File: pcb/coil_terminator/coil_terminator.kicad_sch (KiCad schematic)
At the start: 2 parts, among them J1 Conn_Coaxial

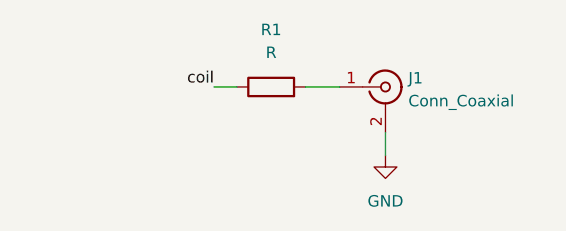
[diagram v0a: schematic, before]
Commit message: added models for compensating coil loss
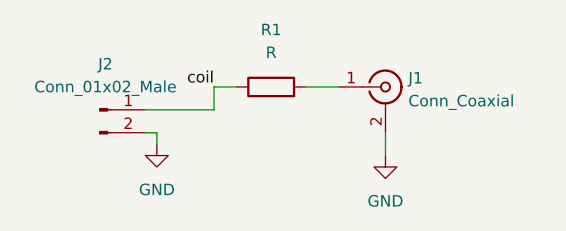
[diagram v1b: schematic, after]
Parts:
- added J2: Conn_01x02_Male, Connector_PinHeader_1.27mm:PinHeader_1x02_P1.27mm_Vertical, symbol Connector:Conn_01x02_Male
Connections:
- net GND: now also J2.2 (Pin_2)
- net coil: now also J2.1 (Pin_1)
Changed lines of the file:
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@@
+    (stroke (width 0) (type default) (color 0 0 0 0))
+  )
+  (wire (pts (xy 73.66 140.97) (xy 74.93 140.97))
+    (stroke (width 0) (type default) (color 0 0 0 0))
+  )
+  (wire (pts (xy 73.66 138.43) (xy 81.28 138.43))
     (stroke (width 0) (type default) (color 0 0 0 0))
   )
@@
     (stroke (width 0) (type default) (color 0 0 0 0))
   )
+  (wire (pts (xy 81.28 138.43) (xy 81.28 135.89))
+    (stroke (width 0) (type default) (color 0 0 0 0))
+  )
+  (wire (pts (xy 74.93 140.97) (xy 74.93 142.24))
+    (stroke (width 0) (type default) (color 0 0 0 0))
+  )
   (label "coil" (at 81.28 135.89 180)
     (effects (font (size 1.27 1.27)) (justify right bottom))
+  )
+  (symbol (lib_id "Connector:Conn_01x02_Male") (at 68.58 138.43 0) (unit 1)
+    (in_bom yes) (on_board yes) (fields_autoplaced)
+    (property "Reference" "J2" (id 0) (at 69.215 133.35 0))
+    (property "Value" "Conn_01x02_Male" (id 1) (at 69.215 135.89 0))
+    (property "Footprint" "Connector_PinHeader_1.27mm:PinHeader_1x02_P1.27mm_Vertical" (id 2) (at 68.58 138.43 0)
+      (effects (font (size 1.27 1.27)) hide)
+    )
+    (property "Datasheet" "~" (id 3) (at 68.58 138.43 0)
+      (effects (font (size 1.27 1.27)) hide)
+    )
+    (pin "1")
+    (pin "2")
+  )
+  (symbol (lib_id "power:GND") (at 74.93 142.24 0) (unit 1)
+    (in_bom yes) (on_board yes) (fields_autoplaced)
+    (property "Reference" "#PWR0102" (id 0) (at 74.93 148.59 0)
+      (effects (font (size 1.27 1.27)) hide)
+    )
+    (property "Value" "GND" (id 1) (at 74.93 147.32 0))
+    (property "Footprint" "" (id 2) (at 74.93 142.24 0)
+      (effects (font (size 1.27 1.27)) hide)
+    )
+    (property "Datasheet" "" (id 3) (at 74.93 142.24 0)
+      (effects (font (size 1.27 1.27)) hide)
+    )
+    (pin "1")
   )
   (symbol (lib_id "Device:R") (at 87.63 135.89 90) (unit 1)
@@
       (reference "#PWR0101") (unit 1) (value "GND") (footprint "")
     )
+    (path "/2c163029-fe98-4c60-9684-2ac79971150f"
+      (reference "#PWR0102") (unit 1) (value "GND") (footprint "")
+    )
     (path "/e8986c1b-6a59-4b6e-8830-feef4fea6eb3"
       (reference "J1") (unit 1) (value "Conn_Coaxial") (footprint "Connector_Coaxial:U.FL_Hirose_U.FL-R-SMT-1_Vertical")
     )
+    (path "/1bb3c75d-6d0d-420b-b38e-d8a4942d0299"
+      (reference "J2") (unit 1) (value "Conn_01x02_Male") (footprint "Connector_PinHeader_1.27mm:PinHeader_1x02_P1.27mm_Vertical")
+    )
     (path "/881b1d90-ad29-476b-96a7-7b4c1c1734ef"
